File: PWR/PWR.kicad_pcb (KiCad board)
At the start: 2 copper layers, 75.2 x 70.1 mm, 21 parts, among them J1 +12v, P1 +5v, P2 GND, SW1 SPDT

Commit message: PCB: starting over...
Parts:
- removed BT1: +9v, XS:Power-Keystone-9v-Battery-Holder
- removed C1: 100uf, XS:Capacitor-Vishay-515D-8mm
- removed C2: 0.33uf, XS:Capacitor-Murata-RCE-Series-5mm
- removed C3: 0.1uf, XS:Capacitor-Murata-RCE-Series-5mm
- removed C4: 10uf, XS:Capacitor-Vishay-515D-5mm
- removed D1, D2: 1N4001, XS:Diode-DO-41
- removed DS1: GREEN, XS:LED-T1-3-4-5mm
- removed DS2: ORANGE, XS:LED-T1-3-4-5mm
- removed DS3: RED, XS:LED-T1-3-4-5mm
- removed J1: +12v, XS:Power-Adafruit-DC-Barrel-Jack
- removed P1: +5v, XS:Connection-Molex-Breakaway-Header-Square-1x1-Simple
- removed P2: GND, XS:Connection-Molex-Breakaway-Header-Square-1x1-Simple
- removed R1, R2: 390, XS:Resistor-Ohmite-OD-Series
- removed R3: 100k, XS:Resistor-Ohmite-OD-Series
- removed SW1: SPDT, XS:Switch-NKK-Series-M-SPDT
- removed VR1: LM7805, XS:Power-Failrchild-LM78XX-TO-220
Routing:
- net Net-(C1-Pad2): track 129.8 -> 0.00 mm
- net Net-(D1-Pad2): track 96.3 -> 0.00 mm
- net Net-(J1-Pad2): track 83.0 -> 0.00 mm
- net Net-(BT1-Pad1): track 74.9 -> 0.00 mm, vias 1 -> 0
- net Net-(C3-Pad1): track 72.9 -> 0.00 mm, vias 2 -> 0
- net Net-(R3-Pad1): track 46.9 -> 0.00 mm, vias 2 -> 0
- net Net-(C1-Pad1): track 39.0 -> 0.00 mm
- net Net-(BT1-Pad2): track 19.7 -> 0.00 mm
- net Net-(DS3-Pad1): track 10.4 -> 0.00 mm
- net Net-(DS1-Pad1): track 10.4 -> 0.00 mm
- net Net-(DS2-Pad1): track 10.2 -> 0.00 mm
- removed copper zone on B.Cu, net Net-(C1-Pad2)
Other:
- net class Default: clearance 0.381 -> 0.254; via_dia 0.635 -> 0.762
- rule trace_clearance: 0.381 -> 0.254
- rule trace_min: 0.381 -> 0.1524
- rule via_min_drill: 0.381 -> 0.3302

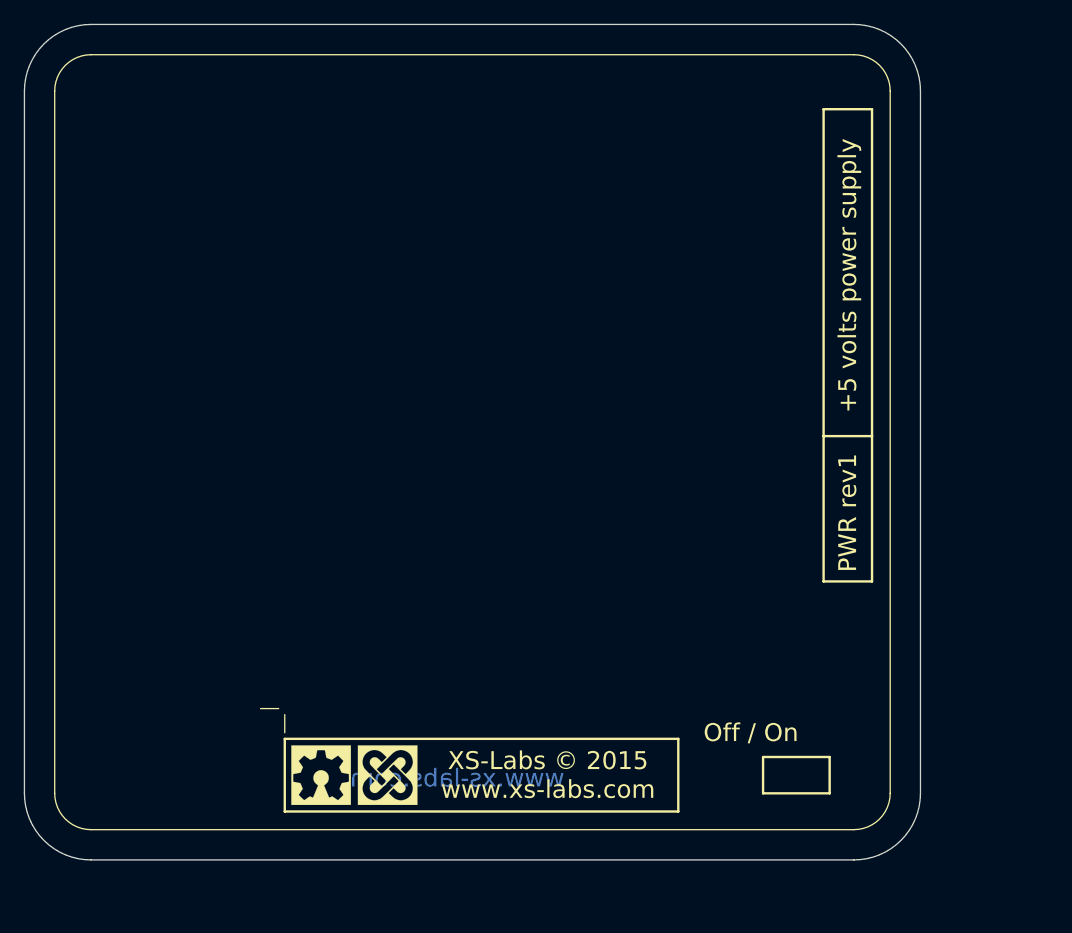
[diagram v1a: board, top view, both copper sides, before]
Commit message: PCB - Placement.
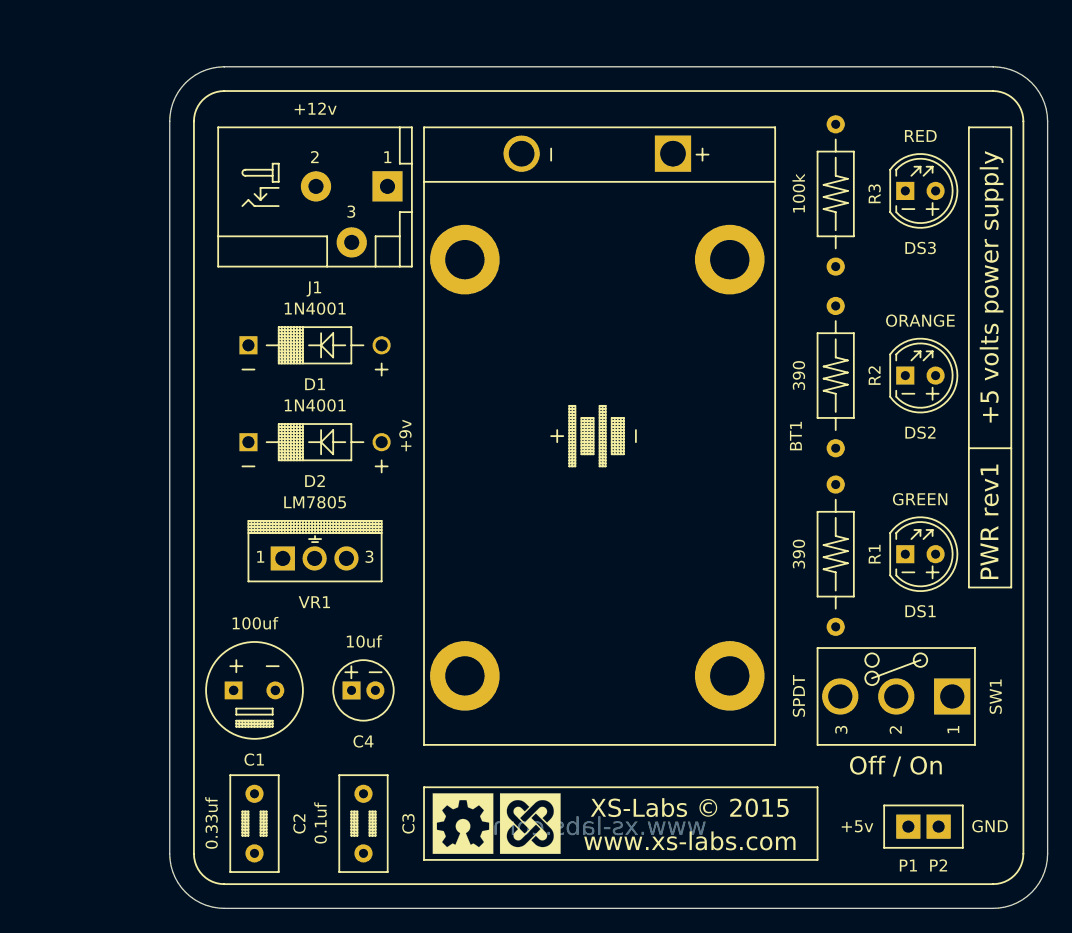
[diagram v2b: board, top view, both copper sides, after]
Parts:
- removed the G*** at (122.4, 126.0)
- removed the G*** at (128.0, 126.0)
- added BT1: +9v, XS:Power-Keystone-9v-Battery-Holder, F.Cu at (145.8, 97.5)
- added C1: 100uf, XS:Capacitor-Vishay-515D-8mm, F.Cu at (116.8, 118.9)
- added C2: 0.33uf, XS:Capacitor-Murata-RCE-Series-5mm, F.Cu at (116.8, 130.0)
- added C3: 0.1uf, XS:Capacitor-Murata-RCE-Series-5mm, F.Cu at (126.0, 130.0)
- added C4: 10uf, XS:Capacitor-Vishay-515D-5mm, F.Cu at (126.0, 118.9)
- added D1: 1N4001, XS:Diode-DO-41, F.Cu at (121.9, 89.9)
- added D2: 1N4001, XS:Diode-DO-41, F.Cu at (121.9, 98.0)
- added DS1: GREEN, XS:LED-T1-3-4-5mm, F.Cu at (172.7, 107.4)
- added DS2: ORANGE, XS:LED-T1-3-4-5mm, F.Cu at (172.7, 92.5)
- added DS3: RED, XS:LED-T1-3-4-5mm, F.Cu at (172.7, 77.0)
- added G***: LOGO, XS:Logo-XS-OSHW-Copyright, F.Cu at (137.2, 130.0)
- added J1: +12v, XS:Power-Adafruit-DC-Barrel-Jack, F.Cu at (121.9, 76.7)
- added P1: +5v, XS:Connection-Molex-Breakaway-Header-Square-1x1-Simple, F.Cu at (171.7, 130.3)
- added P2: GND, XS:Connection-Molex-Breakaway-Header-Square-1x1-Simple, F.Cu at (174.2, 130.3)
- added R1: 390, XS:Resistor-Ohmite-OD-Series, F.Cu at (165.6, 107.4)
- added R2: 390, XS:Resistor-Ohmite-OD-Series, F.Cu at (165.6, 92.5)
- added R3: 100k, XS:Resistor-Ohmite-OD-Series, F.Cu at (165.6, 77.2)
- added SW1: SPDT, XS:Switch-NKK-Series-M-SPDT, F.Cu at (170.7, 119.4)
- added VR1: LM7805, XS:Power-Failrchild-LM78XX-TO-220, F.Cu at (121.9, 107.7)
- moved G*** 12.0 mm to (145.8, 100.1)
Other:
- board size 75.2 x 70.1 mm -> 73.7 x 70.6 mm
- board text removed: "XS-Labs © 2015 www.xs-labs.com"

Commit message: Routing...
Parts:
- moved DS1 0.25 mm to (172.7, 107.7)
- moved R1 0.25 mm to (165.6, 107.7)
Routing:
- net Net-(C1-Pad2): track 0.00 -> 125.0 mm, vias 0 -> 2
- net Net-(D1-Pad2): track 0.00 -> 109.7 mm
- net Net-(J1-Pad2): track 0.00 -> 88.4 mm
- net Net-(BT1-Pad1): track 0.00 -> 75.1 mm
- net Net-(C3-Pad1): track 0.00 -> 70.6 mm, vias 0 -> 2
- net Net-(C1-Pad1): track 0.00 -> 41.3 mm
- net Net-(R3-Pad1): track 0.00 -> 39.2 mm
- net Net-(BT1-Pad2): track 0.00 -> 17.3 mm
- net Net-(DS2-Pad1): track 0.00 -> 10.5 mm
- net Net-(DS1-Pad1): track 0.00 -> 10.5 mm
- net Net-(DS3-Pad1): track 0.00 -> 10.2 mm
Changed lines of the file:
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@@
   (general
     (links 26)
-    (no_connects 26)
-    (area 105.105999 90.881999 178.866001 161.594001)
+    (no_connects 1)
+    (area 109.677999 66.497999 183.438001 137.210001)
     (thickness 1.6)
     (drawings 31)
-    (tracks 0)
+    (tracks 86)
     (zones 0)
     (modules 20)
@@
   )
   (module XS:LED-T1-3-4-5mm (layer F.Cu)
-    (at 172.72 107.442)
+    (at 172.72 107.696)
     (fp_text reference DS1 (at 0 4.826) (layer F.SilkS)
       (effects (font (size 1 1) (thickness 0.15)))
@@
   )
   (module XS:Resistor-Ohmite-OD-Series (layer F.Cu)
-    (at 165.608 107.442 90)
+    (at 165.608 107.696 90)
     (fp_text reference R1 (at 0 3.302 90) (layer F.SilkS)
       (effects (font (size 1 1) (thickness 0.15)))
@@
     (effects (font (size 1.5 1.5) (thickness 0.3)) (justify left))
   )
+  (segment (start 125 81.282) (end 129.03 81.282) (width 0.762) (layer B.Cu) (net 1))
+  (segment (start 136.4742 73.8378) (end 139.2555 73.8378) (width 0.762) (layer B.Cu) (net 1))
+  (segment (start 129.03 81.282) (end 136.4742 73.8378) (width 0.762) (layer B.Cu) (net 1))
+  (segment (start 127.508 98.044) (end 130.81 94.742) (width 0.762) (layer B.Cu) (net 2))
+  (segment (start 146.7993 78.994) (end 151.9555 73.8378) (width 0.762) (layer B.Cu) (net 2))
+  (segment (start 132.842 78.994) (end 146.7993 78.994) (width 0.762) (layer B.Cu) (net 2))
+  (segment (start 130.81 81.026) (end 132.842 78.994) (width 0.762) (layer B.Cu) (net 2))
+  (segment (start 130.81 94.742) (end 130.81 81.026) (width 0.762) (layer B.Cu) (net 2))
+  (segment (start 151.9555 73.8378) (end 151.9555 73.8505) (width 0.762) (layer B.Cu) (net 2))
+  (segment (start 173.99 92.456) (end 173.99 87.63) (width 0.762) (layer B.Cu) (net 2))
+  (segment (start 160.1978 73.8378) (end 151.9555 73.8378) (width 0.762) (layer B.Cu) (net 2))
+  (segment (start 173.99 87.63) (end 160.1978 73.8378) (width 0.762) (layer B.Cu) (net 2))
+  (segment (start 115.09 118.872) (end 115.09 125.798) (width 0.762) (layer B.Cu) (net 3))
+  (segment (start 116.332 98.044) (end 116.332 104.914) (width 0.762) (layer B.Cu) (net 3))
+  (segment (start 116.332 104.914) (end 119.216 107.798) (width 0.762) (layer B.Cu) (net 3))
+  (segment (start 119.216 107.798) (end 119.216 114.746) (width 0.762) (layer B.Cu) (net 3))
+  (segment (start 119.216 114.746) (end 115.09 118.872) (width 0.762) (layer B.Cu) (net 3))
+  (segment (start 116.332 89.916) (end 116.332 98.044) (width 0.762) (layer B.Cu) (net 3))
+  (segment (start 115.09 125.798) (end 116.84 127.548) (width 0.762) (layer B.Cu) (net 3))
+  (segment (start 129.54 122.174) (end 129.54 128.992) (width 0.762) (layer B.Cu) (net 4))
+  (segment (start 129.54 128.992) (end 125.984 132.548) (width 0.762) (layer B.Cu) (net 4))
+  (segment (start 118.618 118.872) (end 121.92 122.174) (width 0.762) (layer B.Cu) (net 4))
+  (segment (start 123.444 122.174) (end 128.524 122.174) (width 0.762) (layer F.Cu) (net 4))
+  (via (at 128.524 122.174) (size 0.762) (drill 0.381) (layers F.Cu B.Cu) (net 4))
+  (segment (start 128.524 122.174) (end 129.54 122.174) (width 0.762) (layer B.Cu) (net 4))
+  (segment (start 129.54 121.412) (end 129.54 122.174) (width 0.762) (layer B.Cu) (net 4))
+  (via (at 123.444 122.174) (size 0.762) (drill 0.381) (layers F.Cu B.Cu) (net 4))
+  (segment (start 127 118.872) (end 129.54 121.412) (width 0.762) (layer B.Cu) (net 4))
+  (segment (start 121.92 122.174) (end 123.444 122.174) (width 0.762) (layer B.Cu) (net 4))
+  (segment (start 125.984 132.548) (end 116.84 132.548) (width 0.762) (layer B.Cu) (net 4))
+  (segment (start 126.984 118.872) (end 128.524 118.872) (width 0.762) (layer B.Cu) (net 4))
+  (segment (start 128.524 118.872) (end 132.334002 122.682002) (width 0.762) (layer B.Cu) (net 4))
+  (segment (start 132.334002 122.682002) (end 172.084998 122.682002) (width 0.762) (layer B.Cu) (net 4))
+  (segment (start 172.084998 122.682002) (end 175.387 119.38) (width 0.762) (layer B.Cu) (net 4))
+  (segment (start 126.984 118.872) (end 127 118.872) (width 0.762) (layer B.Cu) (net 4))
+  (segment (start 118.59 118.872) (end 118.618 118.872) (width 0.762) (layer B.Cu) (net 4))
+  (segment (start 165.608 113.792) (end 169.799 113.792) (width 0.762) (layer B.Cu) (net 4))
+  (segment (start 169.799 113.792) (end 175.387 119.38) (width 0.762) (layer B.Cu) (net 4))
+  (segment (start 174.244 130.302) (end 174.244 120.523) (width 0.762) (layer B.Cu) (net 4))
+  (segment (start 174.244 120.523) (end 175.387 119.38) (width 0.762) (layer B.Cu) (net 4))
+  (segment (start 121.886 107.798) (end 121.886 115.576) (width 0.762) (layer B.Cu) (net 4))
+  (segment (start 121.886 115.576) (end 118.59 118.872) (width 0.762) (layer B.Cu) (net 4))
+  (segment (start 128.27 124.968) (end 125.984 127.254) (width 0.762) (layer B.Cu) (net 5))
+  (segment (start 132.079996 123.698004) (end 130.81 124.968) (width 0.762) (layer B.Cu) (net 5))
+  (segment (start 165.1 123.698004) (end 132.079996 123.698004) (width 0.762) (layer B.Cu) (net 5))
+  (segment (start 171.703996 130.302) (end 165.1 123.698004) (width 0.762) (layer B.Cu) (net 5))
+  (via (at 130.81 124.968) (size 0.762) (drill 0.381) (layers F.Cu B.Cu) (net 5))
+  (segment (start 130.81 124.968) (end 128.27 124.968) (width 0.762) (layer F.Cu) (net 5))
+  (via (at 128.27 124.968) (size 0.762) (drill 0.381) (layers F.Cu B.Cu) (net 5))
+  (segment (start 124.984 126.548) (end 125.984 127.548) (width 0.762) (layer B.Cu) (net 5))
+  (segment (start 124.984 118.872) (end 124.984 126.548) (width 0.762) (layer B.Cu) (net 5))
+  (segment (start 125.984 127.254) (end 125.984 127.548) (width 0.762) (layer B.Cu) (net 5))
+  (segment (start 124.556 107.798) (end 124.556 118.444) (width 0.762) (layer B.Cu) (net 5))
+  (segment (start 124.556 118.444) (end 124.984 118.872) (width 0.762) (layer B.Cu) (net 5))
+  (segment (start 171.704 130.302) (end 171.703996 130.302) (width 0.762) (layer B.Cu) (net 5))
+  (segment (start 128 76.582) (end 124.84 76.582) (width 0.762) (layer B.Cu) (net 6))
+  (segment (start 123.016002 85.424002) (end 127.508 89.916) (width 0.762) (layer B.Cu) (net 6))
+  (segment (start 123.016002 78.405998) (end 123.016002 85.424002) (width 0.762) (layer B.Cu) (net 6))
+  (segment (start 124.84 76.582) (end 123.016002 78.405998) (width 0.762) (layer B.Cu) (net 6))
+  (segment (start 173.99 76.962) (end 173.99 73.406) (width 0.762) (layer B.Cu) (net 6))
+  (segment (start 128 73.168) (end 128 76.582) (width 0.762) (layer B.Cu) (net 6))
+  (segment (start 131.572 69.596) (end 128 73.168) (width 0.762) (layer B.Cu) (net 6))
+  (segment (start 170.18 69.596) (end 131.572 69.596) (width 0.762) (layer B.Cu) (net 6))
+  (segment (start 173.99 73.406) (end 170.18 69.596) (width 0.762) (layer B.Cu) (net 6))
+  (segment (start 127.508 77.074) (end 128 76.582) (width 0.762) (layer B.Cu) (net 6))
+  (segment (start 173.99 107.696) (end 177.8 103.886) (width 0.762) (layer B.Cu) (net 6))
+  (segment (start 177.8 80.772) (end 173.99 76.962) (width 0.762) (layer B.Cu) (net 6))
+  (segment (start 177.8 103.886) (end 177.8 80.772) (width 0.762) (layer B.Cu) (net 6))
+  (segment (start 171.45 107.696) (end 171.45 103.886) (width 0.762) (layer B.Cu) (net 7))
+  (segment (start 169.418 101.854) (end 165.608 101.854) (width 0.762) (layer B.Cu) (net 7))
+  (segment (start 171.45 103.886) (end 169.418 101.854) (width 0.762) (layer B.Cu) (net 7))
+  (segment (start 171.45 92.456) (end 171.45 88.646) (width 0.762) (layer B.Cu) (net 8))
+  (segment (start 169.418 86.614) (end 165.608 86.614) (width 0.762) (layer B.Cu) (net 8))
+  (segment (start 171.45 88.646) (end 169.418 86.614) (width 0.762) (layer B.Cu) (net 8))
+  (segment (start 171.45 76.962) (end 171.45 73.406) (width 0.762) (layer B.Cu) (net 9))
+  (segment (start 169.418 71.374) (end 165.608 71.374) (width 0.762) (layer B.Cu) (net 9))
+  (segment (start 171.45 73.406) (end 169.418 71.374) (width 0.762) (layer B.Cu) (net 9))
+  (segment (start 122 76.582) (end 122 102.442) (width 0.762) (layer B.Cu) (net 10))
+  (segment (start 168.402 121.666) (end 170.688 119.38) (width 0.762) (layer B.Cu) (net 10))
+  (segment (start 132.842 121.666) (end 168.402 121.666) (width 0.762) (layer B.Cu) (net 10))
+  (segment (start 130.81 119.634) (end 132.842 121.666) (width 0.762) (layer B.Cu) (net 10))
+  (segment (start 130.81 111.252) (end 130.81 119.634) (width 0.762) (layer B.Cu) (net 10))
+  (segment (start 122 102.442) (end 130.81 111.252) (width 0.762) (layer B.Cu) (net 10))
+  (segment (start 165.608 83.312) (end 162.052 86.868) (width 0.762) (layer B.Cu) (net 11))
+  (segment (start 162.052 115.443) (end 165.989 119.38) (width 0.762) (layer B.Cu) (net 11))
+  (segment (start 162.052 86.868) (end 162.052 115.443) (width 0.762) (layer B.Cu) (net 11))
 )

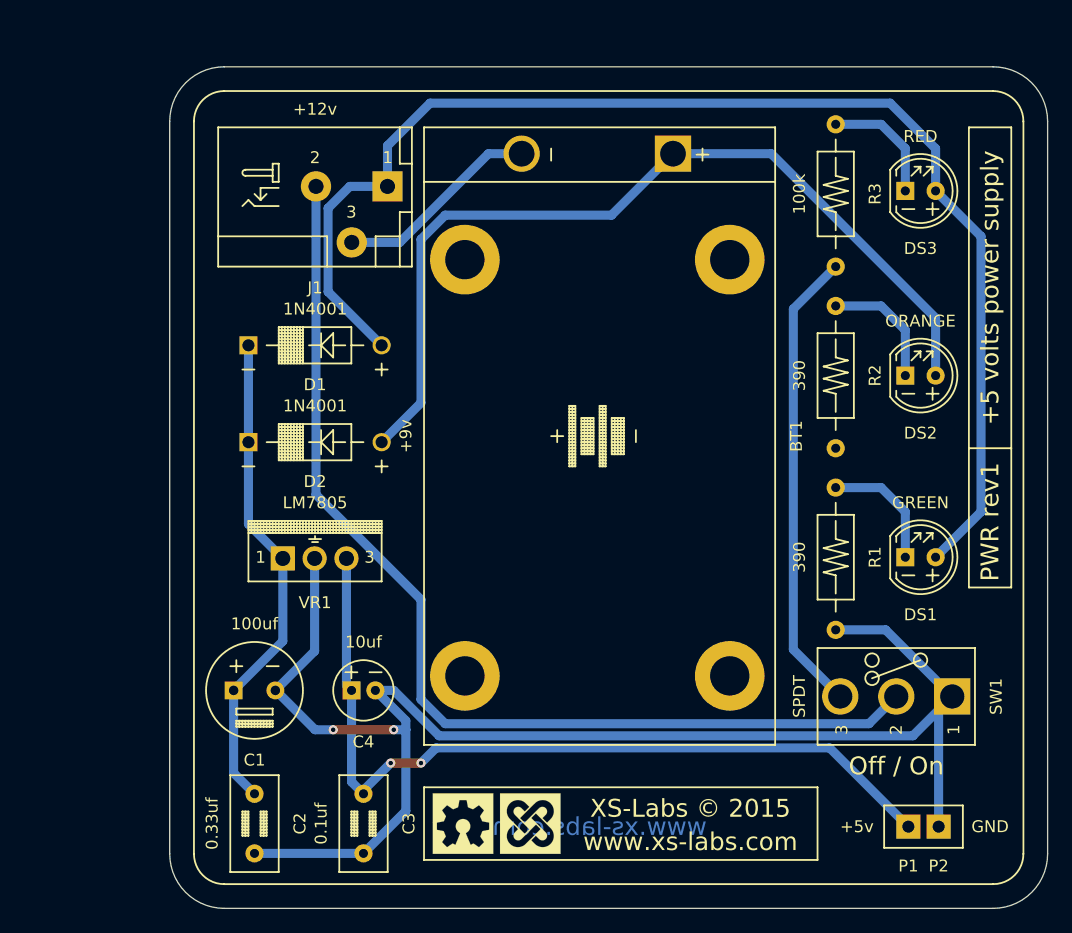
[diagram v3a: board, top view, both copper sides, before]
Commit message: Better routing.
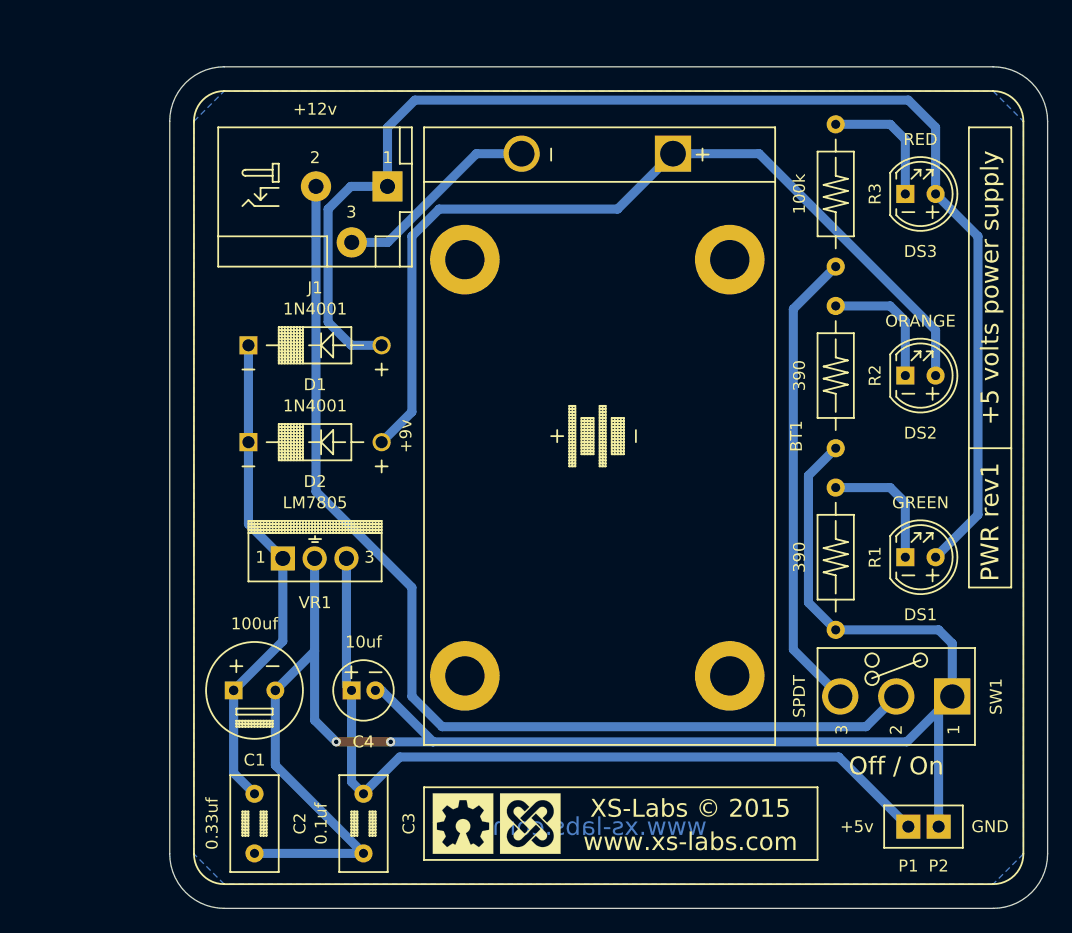
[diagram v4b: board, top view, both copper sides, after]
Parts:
- moved DS3 0.25 mm to (172.7, 77.2)
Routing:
- net Net-(C1-Pad2): track 125.0 -> 149.8 mm
- net Net-(D1-Pad2): track 109.7 -> 112.4 mm
- net Net-(C3-Pad1): track 70.6 -> 69.8 mm, vias 2 -> 0
- net Net-(DS3-Pad1): track 10.2 -> 10.9 mm
- net Net-(J1-Pad2): track 88.4 -> 88.9 mm
- added copper zone on B.Cu, net Net-(J1-Pad2)
